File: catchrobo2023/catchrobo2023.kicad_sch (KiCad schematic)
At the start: 34 parts, among them J1 Conn_01x03_Male, J2 Conn_01x03_Male, J3 Conn_01x03_Male, J4 Conn_01x04_Male, J5 Conn_01x04_Male, J6 Conn_01x02_Male, J7 Conn_01x02_Male, SW1 SW_DPDT_x2, SW2 SW_DIP_x04, U1 942H-2C-9DS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

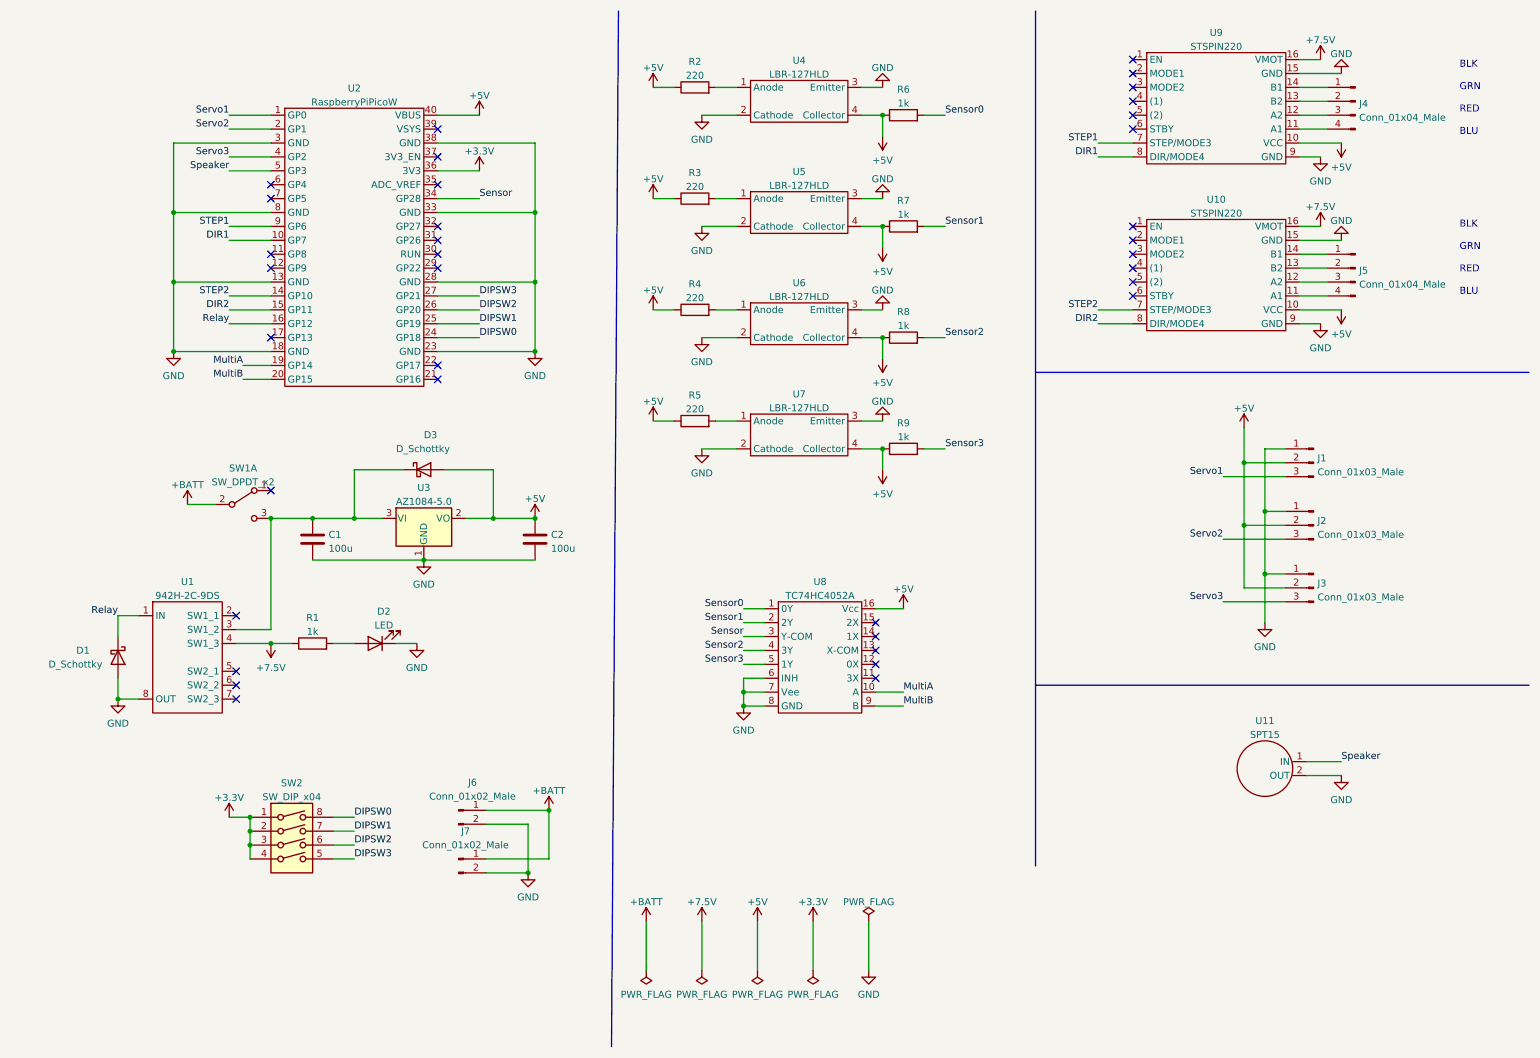
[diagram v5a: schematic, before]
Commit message: 回路図、部品選定が一旦終了
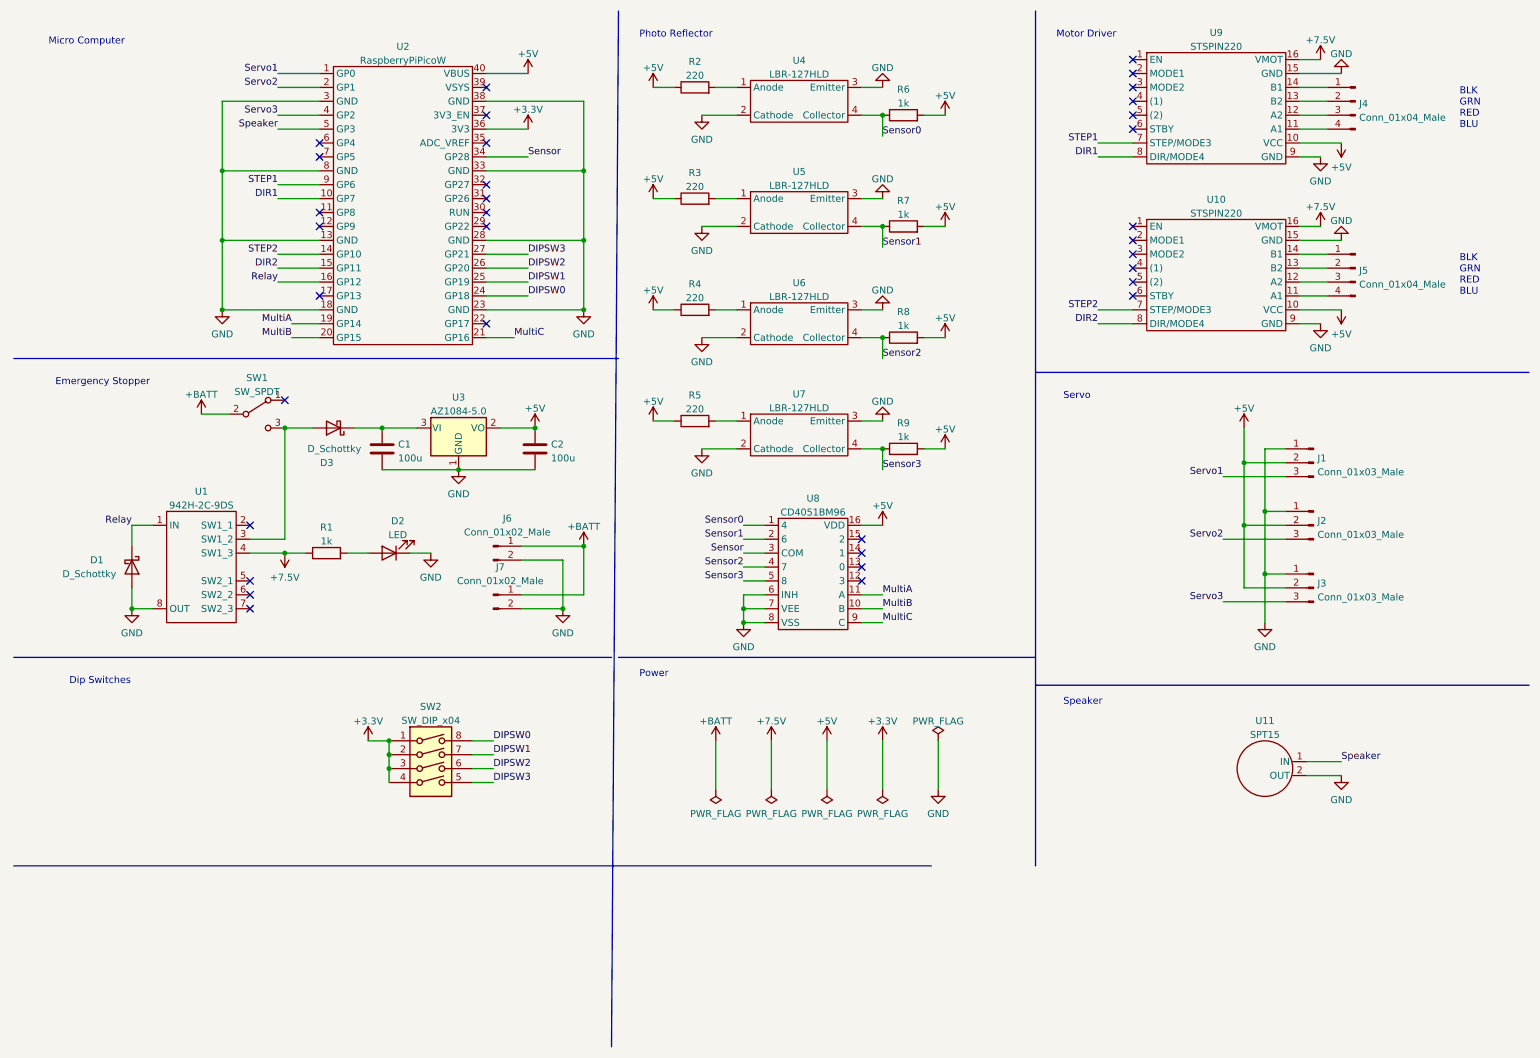
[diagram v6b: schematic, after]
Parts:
- removed SW1: SW_DPDT_x2, symbol Switch:SW_DPDT_x2
- removed U8: TC74HC4052A, Package_DIP:DIP-16_W7.62mm_Socket, symbol catchrobo_parts:TC74HC4052A
- added SW1: SW_SPDT, Catchrobo_parts:2MS1-T1-B4-M2-Q-E-S, symbol Switch:SW_SPDT
- added U8: CD4051BM96, Catchrobo_parts:SOIC-16-150mil, symbol catchrobo_parts:CD4051BM96
- D3: footprint (none) -> Diode_SMD:D_SMA; LCSC (none) -> C22452
- J1, J2, J3: footprint Connector_JST:JST_XH_S3B-XH-A-1_1x03_P2.50mm_Horizontal -> Connector_PinHeader_2.54mm:PinHeader_1x03_P2.54mm_Vertical
- U1: footprint (none) -> Catchrobo_parts:942H-2C-9DS
- U2: footprint (none) -> Catchrobo_parts:RaspberryPiPico
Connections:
- net +5V: now also R6.2, R7.2, R8.2, R9.2, U8.16 (VDD); no longer D3.2 (A), R6.1, R7.1, R8.1, R9.1, U4.4 (Collector), U5.4 (Collector), U6.4 (Collector), U7.4 (Collector)
- net +BATT: now also SW1.2 (B)
- net GND: now also U8.6 (INH), U8.7 (VEE), U8.8 (VSS)
- net MultiA: now also U8.11 (A)
- net MultiB: now also U8.10 (B)
- net Sensor: now also U8.3 (COM)
- net Sensor0: now also R6.1, U4.4 (Collector), U8.1 (4); no longer R6.2
- net Sensor1: now also R7.1, U5.4 (Collector), U8.2 (6); no longer R7.2
- net Sensor2: now also R8.1, U6.4 (Collector), U8.4 (7); no longer R8.2
- net Sensor3: now also R9.1, U7.4 (Collector), U8.5 (8); no longer R9.2
- net at C1.1, D3.1 (K), U3.3 (VI): no longer U1.3 (SW1_2)
- net MultiC: now reaches U2.21 (GP16)
- net MultiC: now also U8.9 (C)
- new net: D3.2 (A), SW1.3 (C), U1.3 (SW1_2)
- no-connect marks 36 -> 34
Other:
- note added: "Dip Switches"
- note added: "Emergency Stopper"
- note added: "Micro Computer"
- note added: "Motor Driver"
- note added: "Photo Reflector"
- note added: "Power"
- note added: "Servo"
- note added: "Speaker"
- moved on the sheet: C1, C2, D1, D2, D3, J6, J7, R1, SW2, U1, U2, U3

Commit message: 遠隔非常停止に使用するリレーをFETに変更
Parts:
- removed D1: D_Schottky, Diode_SMD:D_SOD-323, symbol Device:D_Schottky
- removed U1: 942H-2C-9DS, Catchrobo_parts:942H-2C-9DS, symbol catchrobo_parts:942H-2C-9DS
- added Q1: AO3401A, Package_TO_SOT_SMD:SOT-23, symbol Transistor_FET:AO3401A
- added R10: 330, Resistor_SMD:R_0201_0603Metric, symbol Device:R
- added R11: 10k, Resistor_SMD:R_0201_0603Metric, symbol Device:R
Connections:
- net +7.5V: now also C1.1, D3.1 (K), U3.3 (VI); no longer R1.1, U10.16 (VMOT), U9.16 (VMOT)
- net at D3.2 (A), SW1.3 (C): now also Q1.2 (S), R11.1
- net at D2.2 (A): now also R1.1; no longer R1.2
- net Relay renamed Stopper
- net Stopper: now also R1.2, R10.1
- new net: Q1.1 (G), R10.2, R11.2
- new net MD_Power: Q1.3 (D), U10.16 (VMOT), U9.16 (VMOT)
- no-connect marks 34 -> 30
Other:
- moved on the sheet: D2, R1, SW1, SW2

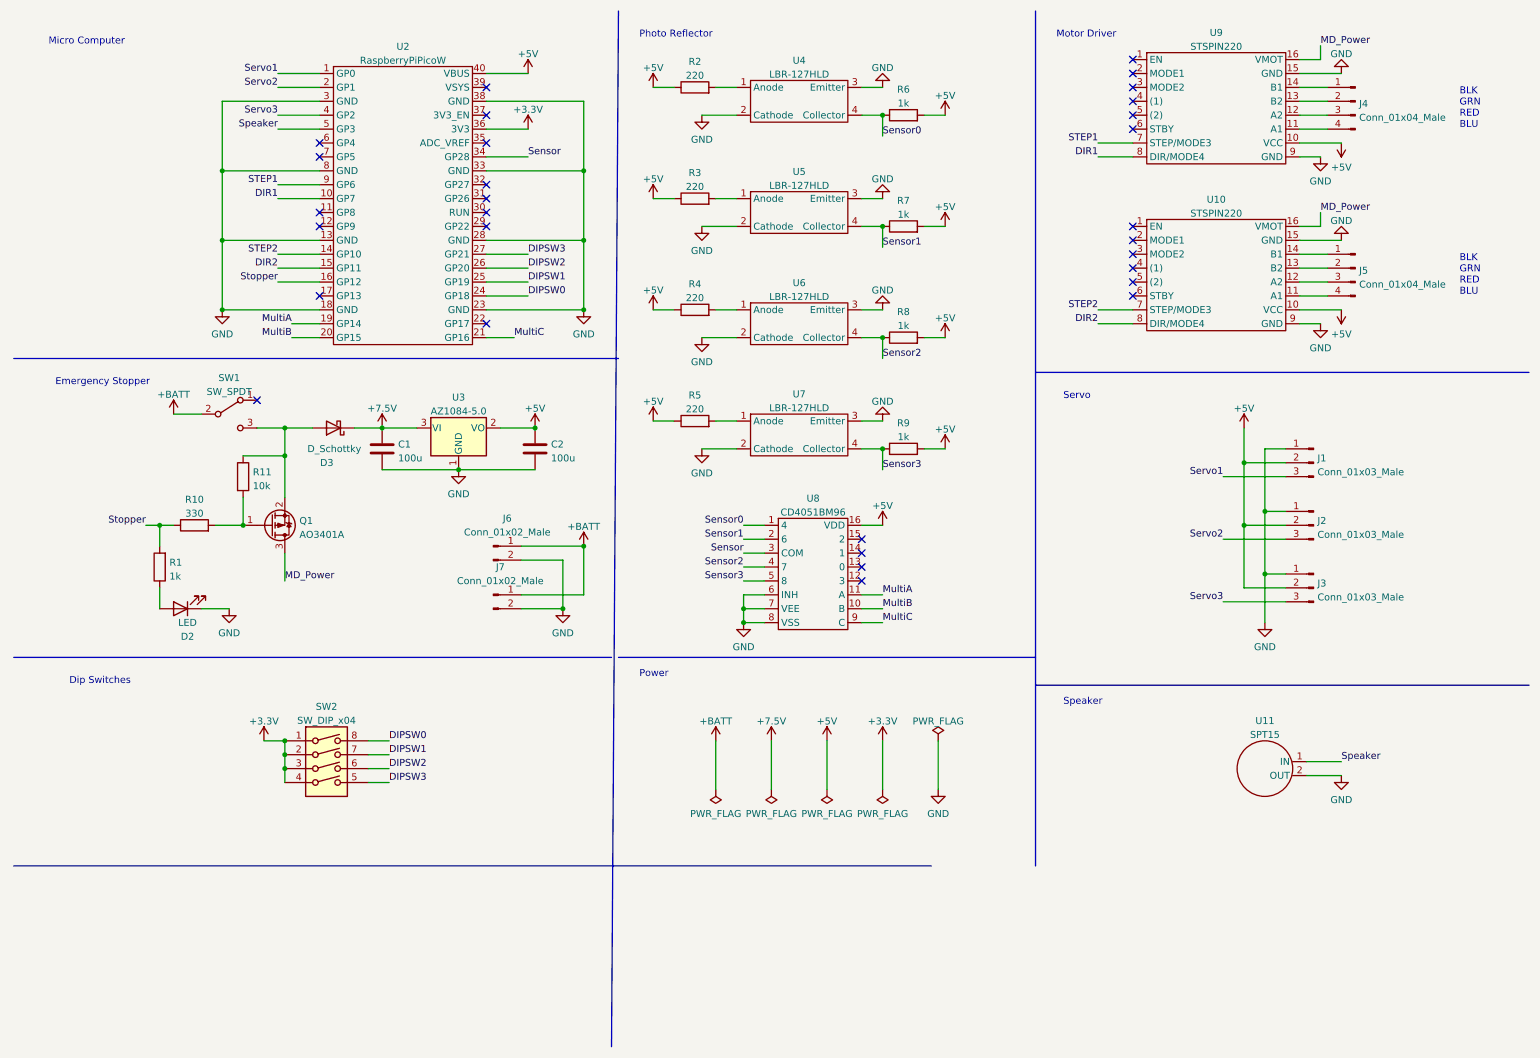
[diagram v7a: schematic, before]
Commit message: メイン基板作成途中
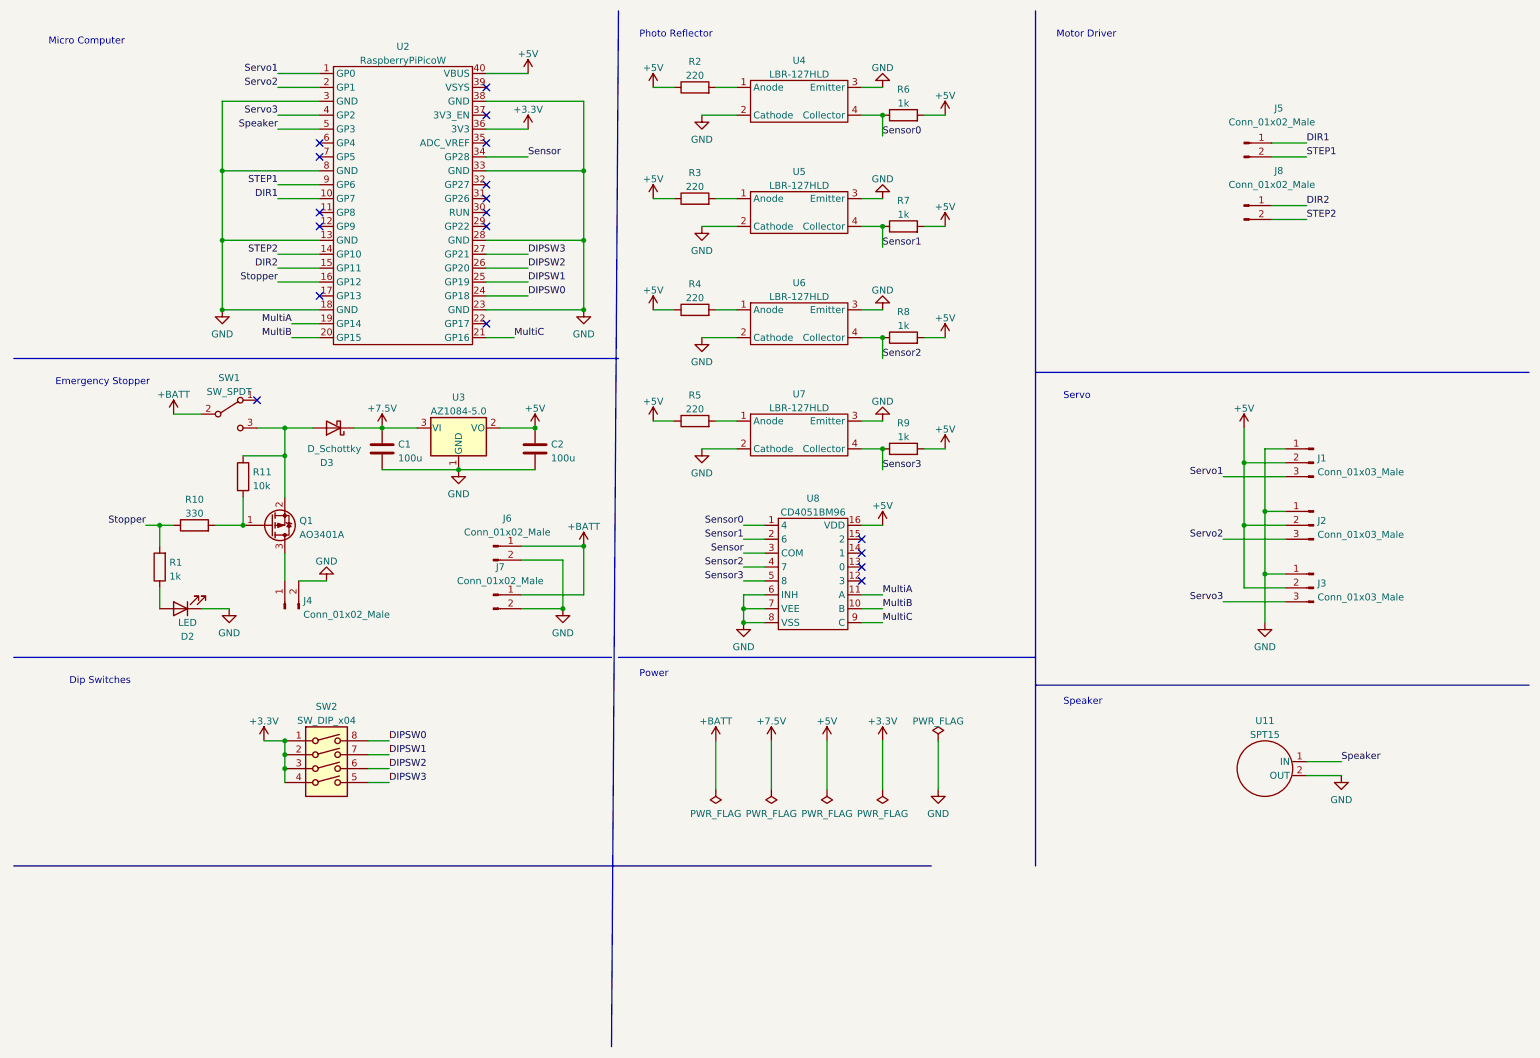
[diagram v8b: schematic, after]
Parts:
- removed J4, J5: Conn_01x04_Male, Connector_JST:JST_XH_S4B-XH-A-1_1x04_P2.50mm_Horizontal, symbol Connector:Conn_01x04_Male
- removed U10, U9: STSPIN220, Catchrobo_parts:STSPIN220, symbol catchrobo_parts:STSPIN220
- added J4, J5, J8: Conn_01x02_Male, Connector_JST:JST_XH_B2B-XH-AM_1x02_P2.50mm_Vertical, symbol Connector:Conn_01x02_Male
- J6, J7, U11: footprint Connector_JST:JST_XH_S2B-XH-A-1_1x02_P2.50mm_Horizontal -> Connector_JST:JST_XH_B2B-XH-AM_1x02_P2.50mm_Vertical
- U4, U5, U6, U7: footprint Connector_JST:JST_XH_S2B-XH-A-1_1x02_P2.50mm_Horizontal -> Connector_JST:JST_XH_B4B-XH-AM_1x04_P2.50mm_Vertical
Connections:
- net DIR1: now also J5.1 (Pin_1)
- net DIR2: now also J8.1 (Pin_1)
- net GND: now also J4.2 (Pin_2)
- net STEP1: now also J5.2 (Pin_2)
- net STEP2: now also J8.2 (Pin_2)
- net MD_Power: no longer names the net of Q1.3 (D)
- net MD_Power: now also J4.1 (Pin_1)
- no-connect marks 30 -> 18
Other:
- note removed: "BLK GRN RED BLU"
